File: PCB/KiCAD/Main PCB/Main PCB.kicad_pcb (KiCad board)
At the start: 2 copper layers, 118 x 118 mm, 130 parts, among them IC1 ADG608BRZ, IC2 ADG608BRZ, IC3 VNH7070ASTR, IC4 VNH7070ASTR, IC5 VNH7070ASTR, IC6 VNH7070ASTR, IC7 VNH7070ASTR, IC8 XB3-24Z8CM, J1 Conn_01x04, J10 Conn_01x02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

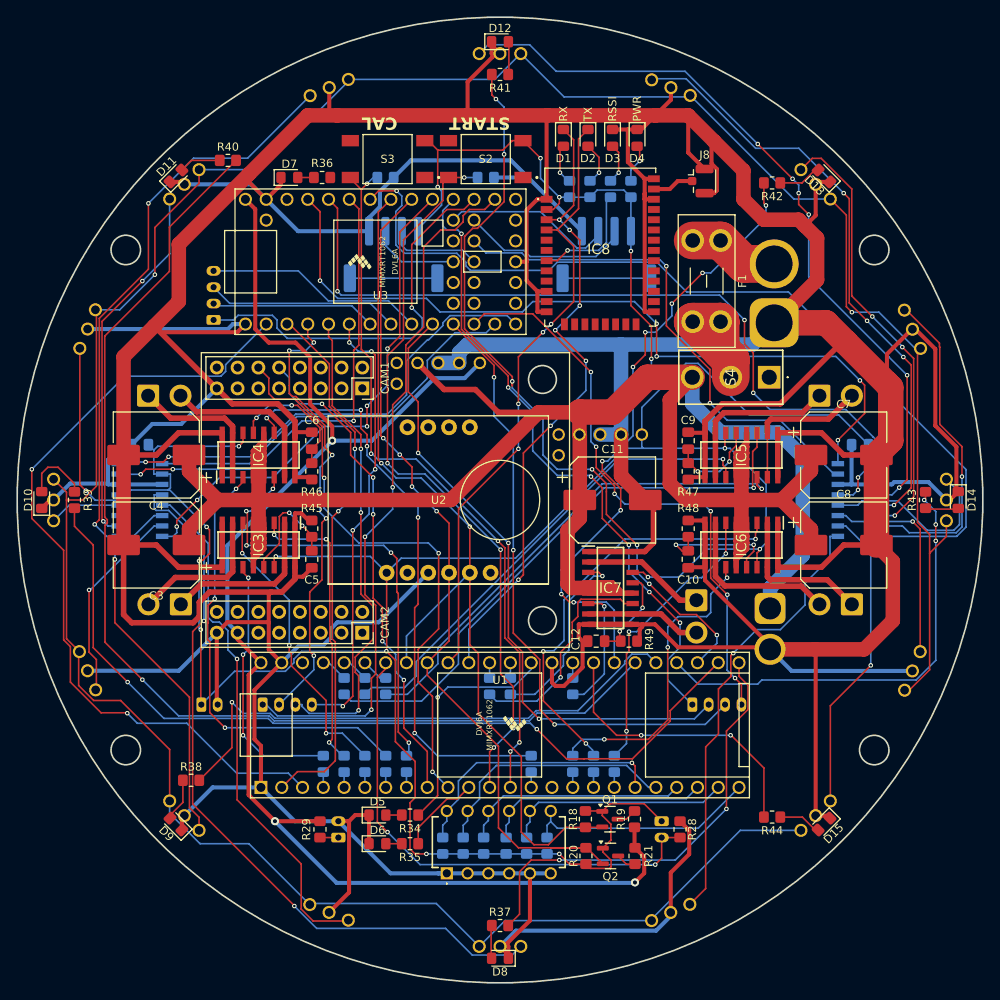
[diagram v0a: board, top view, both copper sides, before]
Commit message: Finished traces and made them curved
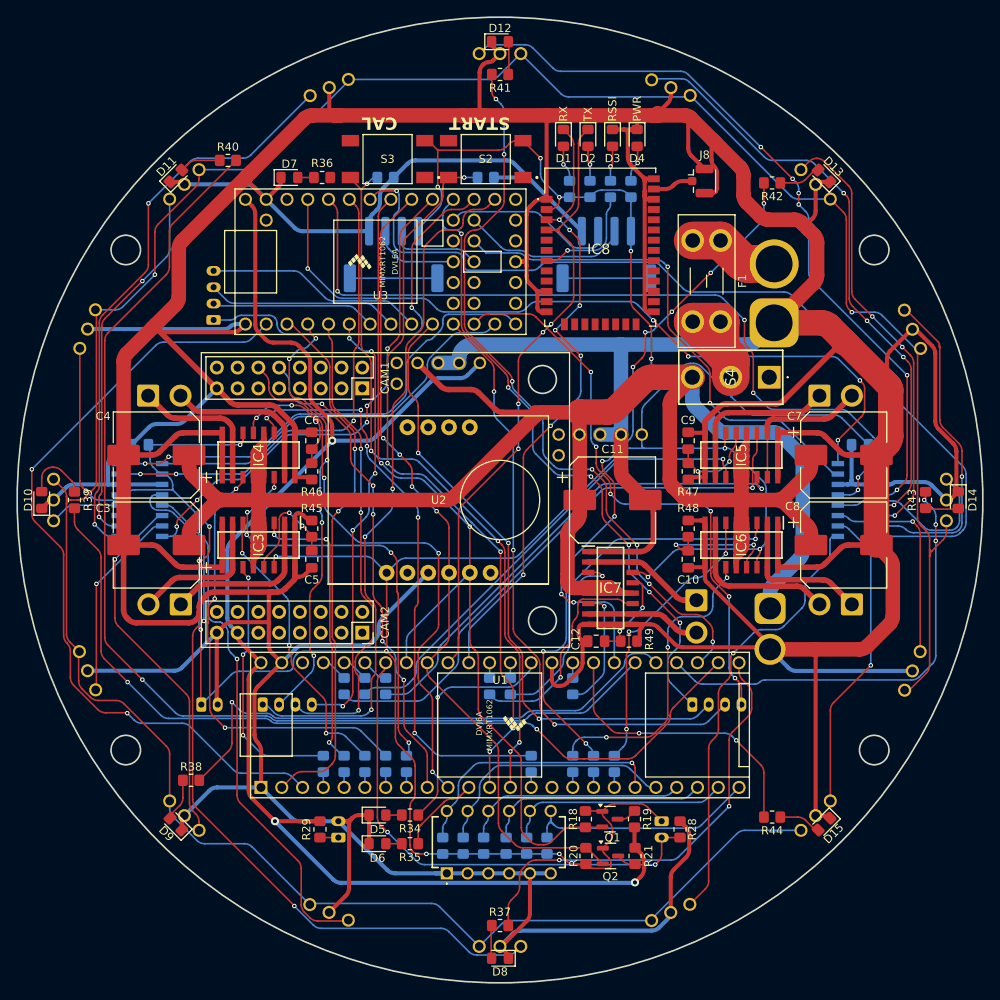
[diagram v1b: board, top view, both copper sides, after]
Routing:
- net +12V: track 305.6 -> 330.8 mm
- net 3V3_SDA: track 105.3 -> 100.5 mm
- net TSSP_2_A1: track 96.7 -> 93.9 mm
- net IR_DIR_225: track 78.0 -> 75.8 mm
- net +3V3: track 380.2 -> 378.3 mm
- net LED_1_A0: track 55.4 -> 53.5 mm
- net IR_DIR_180: track 93.4 -> 91.9 mm
- net IN_B_M2: track 53.6 -> 52.2 mm
- net TEENSY_1_TX: track 98.1 -> 96.9 mm
- net Net-(S4-COM): track 19.7 -> 20.9 mm
- net +5V: track 173.5 -> 172.3 mm
- net LED_2_OUT: track 48.7 -> 47.6 mm
- net GND: track 1076.0 -> 1075.0 mm
- net Net-(D2-A): track 5.31 -> 4.33 mm
- net SPARE_SDA: track 20.6 -> 21.6 mm
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
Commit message: Redone main PCB traces and started lower PCB
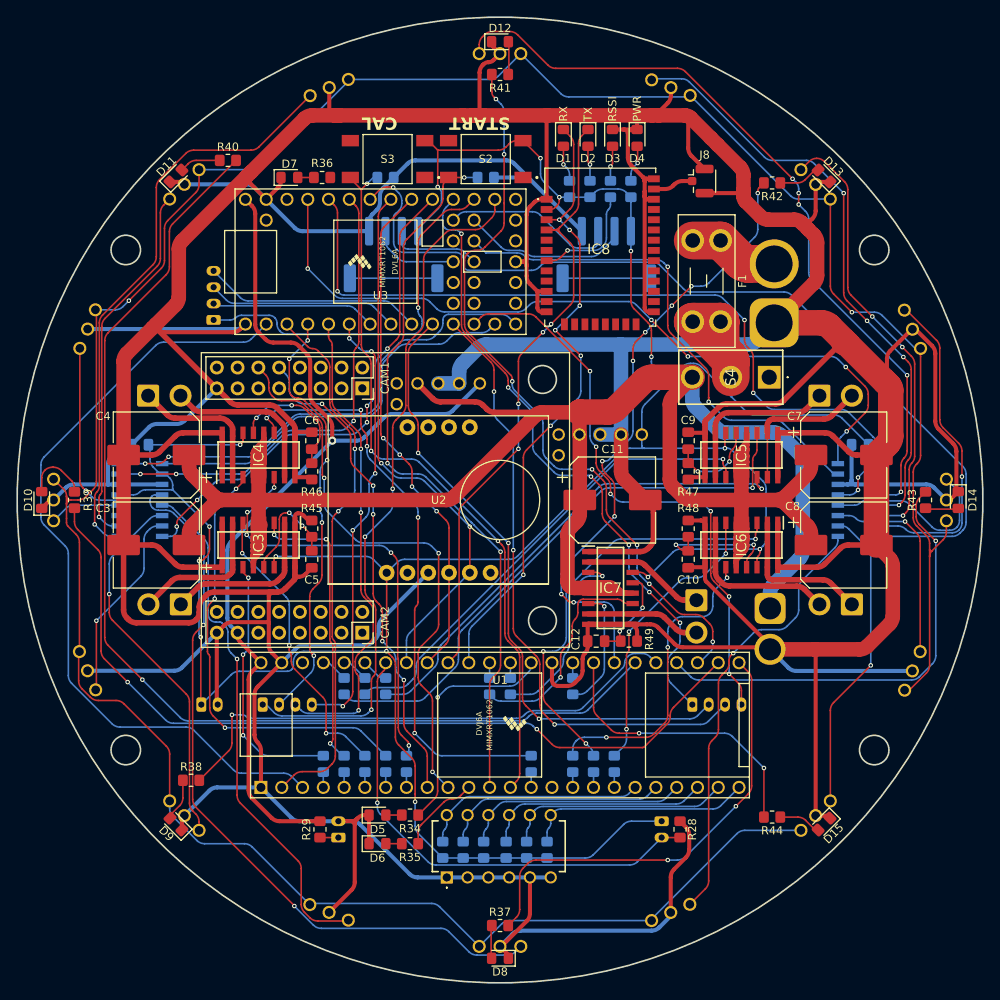
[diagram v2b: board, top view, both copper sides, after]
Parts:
- removed Q1, Q2: BSS138, Package_TO_SOT_SMD:SOT-23
- removed R18, R19, R20, R21: 10k, Resistor_SMD:R_0805_2012Metric_Pad1.20x1.40mm_HandSolder
- IR1, IR10, IR11, IR12, IR13, IR14, IR15, IR16, IR2, IR3, IR4, IR5, IR6, IR7, IR8, IR9: value TSSP4038 -> TSOP34840
- moved U5 2.50 mm to (-9.99, -5.12)
- moved R1 0.50 mm to (-7.00, 42.8)
- moved R10 0.50 mm to (0.75, 42.8)
- moved R11 0.50 mm to (3.25, 42.8)
- moved R16 0.50 mm to (5.75, 42.8)
- moved R2 0.50 mm to (-4.50, 42.8)
- moved R5 0.50 mm to (-2.00, 42.8)
- moved S1 0.50 mm to (-6.50, 46.1)
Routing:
- net +5V: track 172.3 -> 116.7 mm, vias 3 -> 1
- net 3V3_SCL: track 111.7 -> 66.6 mm
- net 3V3_SDA: track 100.5 -> 62.5 mm
- net +3V3: track 378.3 -> 365.5 mm, vias 18 -> 17
- net Net-(U1-27_A13_SCK1): track 32.7 -> 27.7 mm, vias 1 -> 0
- net GND: track 1075.0 -> 1070.2 mm
- net Net-(U1-28_RX7): track 30.7 -> 27.7 mm
- net Net-(IC2-S1): track 91.3 -> 94.0 mm, vias 6 -> 5
- net 5V_SDA: track 2.42 -> 0.00 mm
- net 5V_SCL: track 2.42 -> 0.00 mm
- net LG_RECEIVE: track 61.6 -> 59.4 mm, vias 2 -> 1
- net IR_DIR_45: track 67.4 -> 65.3 mm
- net Net-(U1-32_OUT1B): track 29.4 -> 27.6 mm
- net TSSP_1_A0: track 48.6 -> 50.1 mm
- net START_BUTTON: track 89.8 -> 88.5 mm, vias 5 -> 3
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
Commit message: Started routing lower PCB
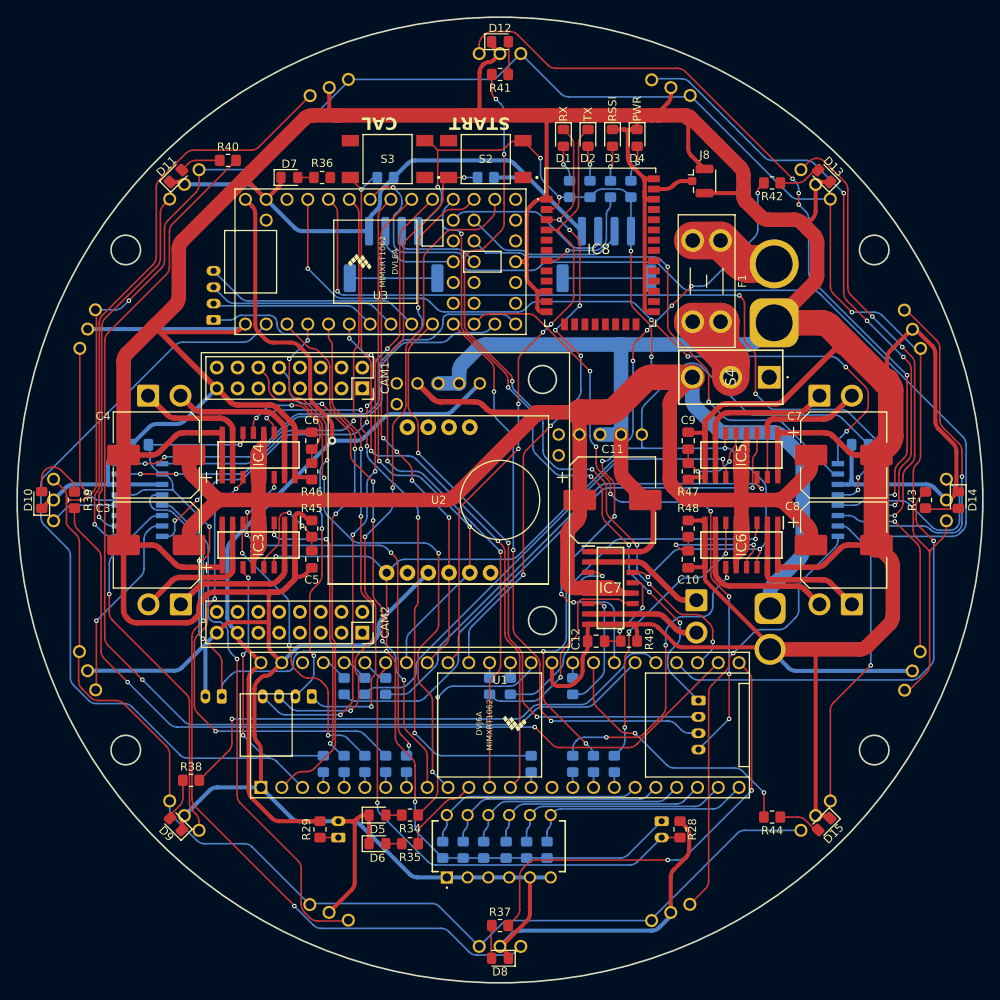
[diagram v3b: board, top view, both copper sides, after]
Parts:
- moved J1 6.08 mm to (-23.0, 24.0), turned to 180 degrees
- moved J10 2.69 mm to (-34.0, 24.0), turned to 180 degrees
- moved J3 0.90 mm to (24.2, 24.5), turned to -90 degrees
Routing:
- net LED_1_A2: track 53.9 -> 61.3 mm
- net LED_3_A2: track 71.4 -> 77.8 mm, vias 6 -> 7
- net LED_1_OUT: track 84.7 -> 78.5 mm
- net LED_3_A1: track 75.4 -> 71.6 mm
- net IR_DIR_315: track 35.5 -> 33.1 mm
- net IN_A_M2: track 53.5 -> 55.6 mm
- net TSSP_2_OUT: track 111.1 -> 113.2 mm
- net LED_3_A0: track 77.1 -> 75.1 mm
- net +3V3: track 365.5 -> 363.5 mm
- net LED_1_A0: track 52.4 -> 50.5 mm
- net LED_1_A1: track 58.2 -> 59.8 mm
- net TEENSY_1_TX: track 96.1 -> 94.7 mm
- net TSSP_2_A0: track 92.3 -> 93.6 mm
- net GND: track 1070.2 -> 1069.1 mm
- net TEENSY_1_RX: track 65.7 -> 64.8 mm
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
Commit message: Added another switch
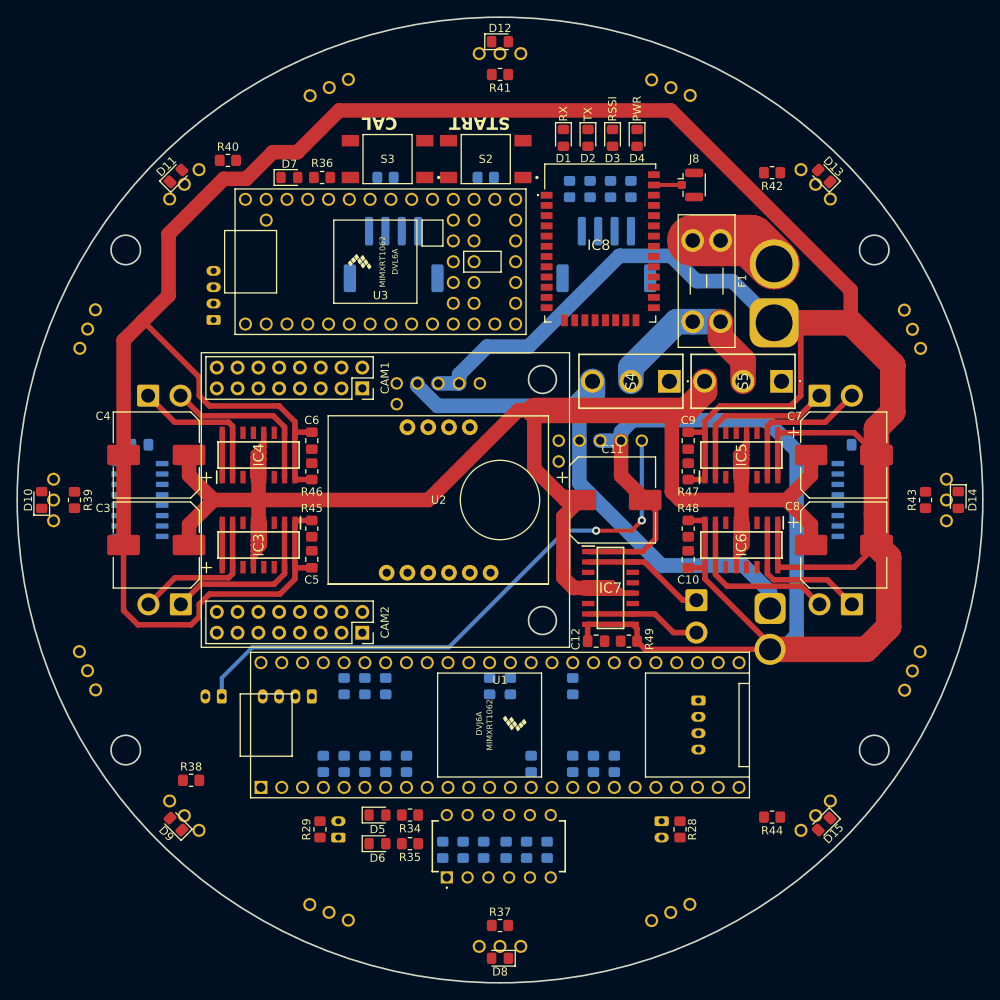
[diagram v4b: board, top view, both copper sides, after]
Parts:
- added S5: 1101M2S3CGE2, 1101M2S3CGE2:1101M2S3CGE2, F.Cu at (34.4, -14.5)
- moved S4 12.2 mm to (20.7, -14.5)
- moved J8 1.36 mm to (23.2, -38.5)
- moved R42 1.25 mm to (33.2, -40.0)
- moved U4 0.75 mm to (9.80, 1.88)
- moved IC8 0.50 mm to (12.2, -23.5)
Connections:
- C11 pad 1: +12V -> +12V_MOTOR
- C3 pad 1: +12V -> +12V_MOTOR
- C4 pad 1: +12V -> +12V_MOTOR
- C7 pad 1: +12V -> +12V_MOTOR
- C8 pad 1: +12V -> +12V_MOTOR
- IC3 pad 12: +12V -> +12V_MOTOR
- IC3 pad 4: +12V -> +12V_MOTOR
- IC3 pad 5: +12V -> +12V_MOTOR
- IC4 pad 12: +12V -> +12V_MOTOR
- IC4 pad 4: +12V -> +12V_MOTOR
- IC4 pad 5: +12V -> +12V_MOTOR
- IC5 pad 12: +12V -> +12V_MOTOR
- IC5 pad 4: +12V -> +12V_MOTOR
- IC5 pad 5: +12V -> +12V_MOTOR
- IC6 pad 12: +12V -> +12V_MOTOR
- IC6 pad 4: +12V -> +12V_MOTOR
- IC6 pad 5: +12V -> +12V_MOTOR
- IC7 pad 12: +12V -> +12V_MOTOR
- IC7 pad 4: +12V -> +12V_MOTOR
- IC7 pad 5: +12V -> +12V_MOTOR
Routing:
- net GND: track 1069.1 -> 547.1 mm
- net TSSP_PWR: track 350.5 -> 0.00 mm, vias 2 -> 0
- net +3V3: track 363.5 -> 71.3 mm, vias 17 -> 2
- net +12V_MOTOR: track 0.00 -> 286.5 mm
- net +12V: track 329.8 -> 65.0 mm
- net IR_DIR_135: track 137.1 -> 0.00 mm, vias 1 -> 0
- net +5V: track 116.7 -> 0.00 mm, vias 1 -> 0
- net TSSP_2_OUT: track 113.2 -> 0.00 mm, vias 1 -> 0
- net IR_DIR_90: track 103.3 -> 0.00 mm, vias 2 -> 0
- net TEENSY_1_TX: track 94.7 -> 0.00 mm
- net TSSP_2_A1: track 94.1 -> 0.00 mm, vias 5 -> 0
- net Net-(IC2-S1): track 93.8 -> 0.00 mm, vias 5 -> 0
- net TSSP_2_A0: track 93.6 -> 0.00 mm, vias 3 -> 0
- net IR_DIR_180: track 91.6 -> 0.00 mm, vias 7 -> 0
- net Net-(IC1-S1): track 91.0 -> 0.00 mm, vias 2 -> 0
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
